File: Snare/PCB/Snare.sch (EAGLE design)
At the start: 97 parts, among them IC1 LM741P, IC2 LM741P, IC3 LM741P, IC4 LM741P, IC5 LM741P, IC6 LM741P, Q1 2N3904, Q2 2N3904, Q3 2N2222A, Q4 2N2222A, Q6 2N3904

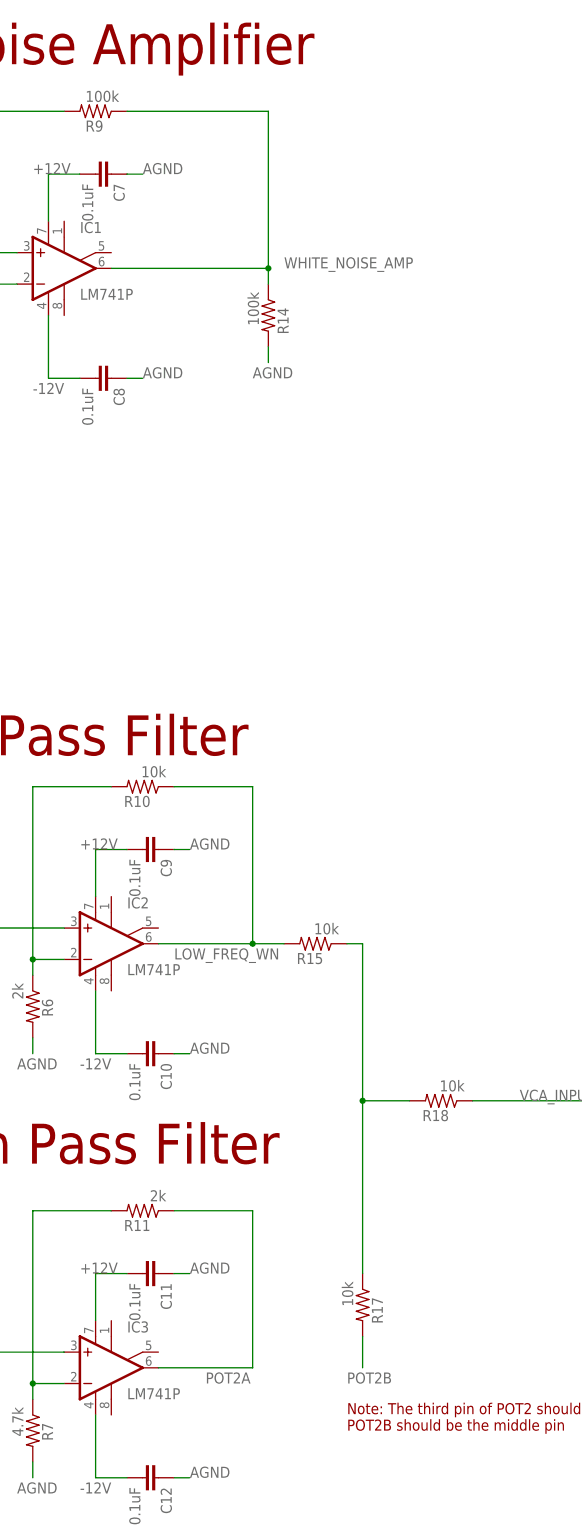
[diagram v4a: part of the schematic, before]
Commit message: Added a few missing components
Added a few missing components. 3 coupling capacitors were missing
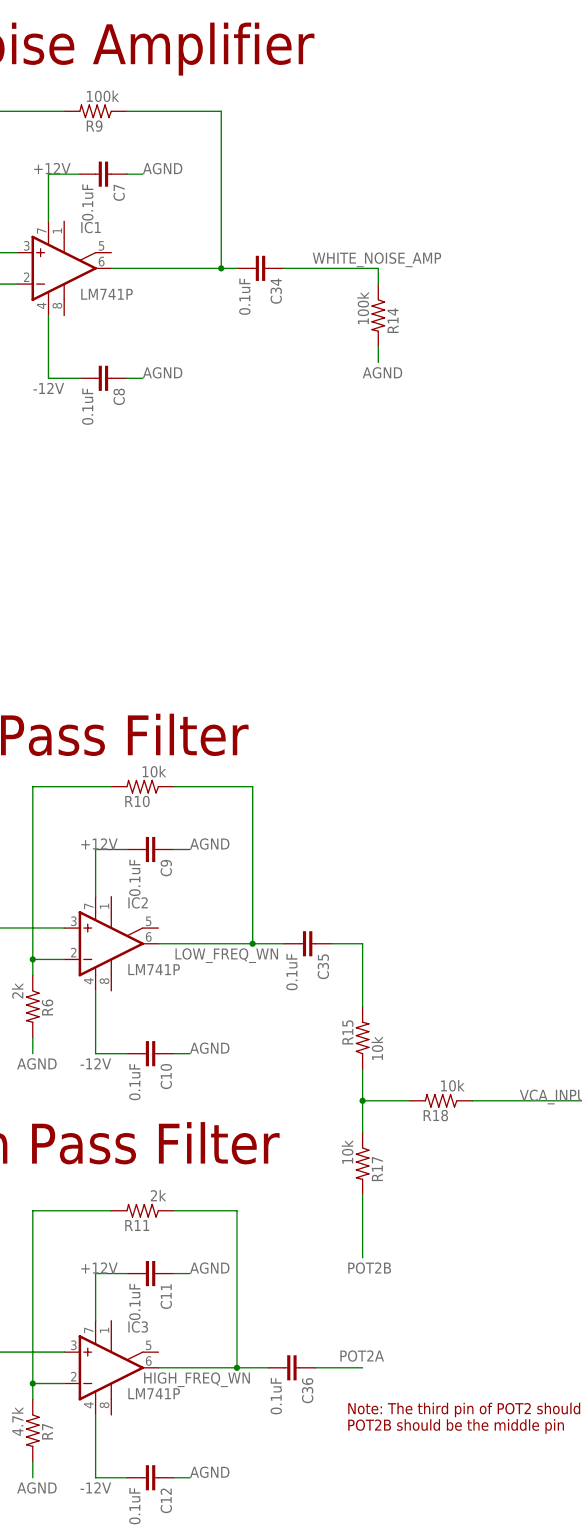
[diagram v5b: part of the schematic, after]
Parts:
- added C34, C35, C36: 0.1uF, resistor:C-EU050-024X044
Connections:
- new net HIGH_FREQ_WN: C36.2, IC3.OUT, R11.1
- new net N$10: C35.1, R15.2
- new net N$9: C34.2, IC1.OUT, R9.1
- net LOW_FREQ_WN: now also C35.2; no longer R15.2
- net POT2A: now also C36.1; no longer IC3.OUT, R11.1
- net WHITE_NOISE_AMP: now also C34.1; no longer IC1.OUT, R9.1
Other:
- moved on the sheet: R14, R15, R17
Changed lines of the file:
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@@
 <part name="J3" library="SparkFun-Connectors" deviceset="CONN_02" device="1X02_NO_SILK"/>
 <part name="J4" library="SparkFun-Connectors" deviceset="CONN_02" device="1X02_NO_SILK"/>
+<part name="C34" library="resistor" library_urn="urn:adsk.eagle:library:348" deviceset="C-EU" device="050-024X044" package3d_urn="urn:adsk.eagle:package:26162/1" value="0.1uF"/>
+<part name="C35" library="resistor" library_urn="urn:adsk.eagle:library:348" deviceset="C-EU" device="050-024X044" package3d_urn="urn:adsk.eagle:package:26162/1" value="0.1uF"/>
+<part name="C36" library="resistor" library_urn="urn:adsk.eagle:library:348" deviceset="C-EU" device="050-024X044" package3d_urn="urn:adsk.eagle:package:26162/1" value="0.1uF"/>
 </parts>
 <sheets>
@@
 <attribute name="VALUE" x="75.438" y="146.05" size="1.778" layer="96" rot="R270"/>
 </instance>
-<instance part="R14" gate="G$1" x="116.84" y="254" smashed="yes" rot="R270">
-<attribute name="NAME" x="118.3386" y="255.27" size="1.778" layer="95" rot="R270"/>
-<attribute name="VALUE" x="113.538" y="257.81" size="1.778" layer="96" rot="R270"/>
-</instance>
-<instance part="R15" gate="G$1" x="124.46" y="152.4" smashed="yes" rot="R180">
-<attribute name="NAME" x="125.73" y="150.9014" size="1.778" layer="95" rot="R180"/>
-<attribute name="VALUE" x="128.27" y="155.702" size="1.778" layer="96" rot="R180"/>
+<instance part="R14" gate="G$1" x="134.62" y="254" smashed="yes" rot="R270">
+<attribute name="NAME" x="136.1186" y="255.27" size="1.778" layer="95" rot="R270"/>
+<attribute name="VALUE" x="131.318" y="257.81" size="1.778" layer="96" rot="R270"/>
+</instance>
+<instance part="R15" gate="G$1" x="132.08" y="137.16" smashed="yes" rot="R90">
+<attribute name="NAME" x="130.5814" y="135.89" size="1.778" layer="95" rot="R90"/>
+<attribute name="VALUE" x="135.382" y="133.35" size="1.778" layer="96" rot="R90"/>
 </instance>
 <instance part="R18" gate="G$1" x="144.78" y="127" smashed="yes" rot="R180">
@@
 <attribute name="VALUE" x="148.59" y="130.302" size="1.778" layer="96" rot="R180"/>
 </instance>
-<instance part="R17" gate="G$1" x="132.08" y="93.98" smashed="yes" rot="R270">
-<attribute name="NAME" x="133.5786" y="95.25" size="1.778" layer="95" rot="R270"/>
-<attribute name="VALUE" x="128.778" y="97.79" size="1.778" layer="96" rot="R270"/>
+<instance part="R17" gate="G$1" x="132.08" y="116.84" smashed="yes" rot="R270">
+<attribute name="NAME" x="133.5786" y="118.11" size="1.778" layer="95" rot="R270"/>
+<attribute name="VALUE" x="128.778" y="120.65" size="1.778" layer="96" rot="R270"/>
 </instance>
 <instance part="IC6" gate="A" x="406.4" y="149.86" smashed="yes">
@@
 <attribute name="VALUE" x="370.84" y="58.674" size="1.778" layer="96" font="vector"/>
 <attribute name="NAME" x="370.84" y="69.088" size="1.778" layer="95" font="vector"/>
+</instance>
+<instance part="C34" gate="G$1" x="116.84" y="261.62" smashed="yes" rot="R270">
+<attribute name="NAME" x="117.221" y="260.096" size="1.778" layer="95" rot="R270"/>
+<attribute name="VALUE" x="112.141" y="260.096" size="1.778" layer="96" rot="R270"/>
+</instance>
+<instance part="C35" gate="G$1" x="124.46" y="152.4" smashed="yes" rot="R270">
+<attribute name="NAME" x="124.841" y="150.876" size="1.778" layer="95" rot="R270"/>
+<attribute name="VALUE" x="119.761" y="150.876" size="1.778" layer="96" rot="R270"/>
+</instance>
+<instance part="C36" gate="G$1" x="121.92" y="83.82" smashed="yes" rot="R270">
+<attribute name="NAME" x="122.301" y="82.296" size="1.778" layer="95" rot="R270"/>
+<attribute name="VALUE" x="117.221" y="82.296" size="1.778" layer="96" rot="R270"/>
 </instance>
 </instances>
@@
 </segment>
 <segment>
-<pinref part="R11" gate="G$1" pin="1"/>
-<wire x1="101.6" y1="109.22" x2="114.3" y2="109.22" width="0.1524" layer="91"/>
-<wire x1="114.3" y1="109.22" x2="114.3" y2="83.82" width="0.1524" layer="91"/>
-<pinref part="IC3" gate="A" pin="OUT"/>
-<wire x1="114.3" y1="83.82" x2="99.06" y2="83.82" width="0.1524" layer="91"/>
-<label x="106.68" y="81.28" size="1.778" layer="95"/>
+<pinref part="C36" gate="G$1" pin="1"/>
+<wire x1="124.46" y1="83.82" x2="132.08" y2="83.82" width="0.1524" layer="91"/>
+<label x="128.27" y="84.836" size="1.778" layer="95"/>
 </segment>
 </net>
@@
 <segment>
 <pinref part="R17" gate="G$1" pin="2"/>
-<wire x1="132.08" y1="88.9" x2="132.08" y2="83.82" width="0.1524" layer="91"/>
-<label x="129.54" y="81.28" size="1.778" layer="95"/>
+<wire x1="132.08" y1="111.76" x2="132.08" y2="101.6" width="0.1524" layer="91"/>
+<label x="129.54" y="99.06" size="1.778" layer="95"/>
 </segment>
 </net>
@@
 <segment>
 <pinref part="R14" gate="G$1" pin="2"/>
-<wire x1="116.84" y1="248.92" x2="116.84" y2="246.38" width="0.1524" layer="91"/>
-<label x="114.3" y="243.84" size="1.778" layer="95"/>
+<wire x1="134.62" y1="248.92" x2="134.62" y2="246.38" width="0.1524" layer="91"/>
+<label x="132.08" y="243.84" size="1.778" layer="95"/>
 </segment>
 <segment>
@@
 <net name="WHITE_NOISE_AMP" class="0">
 <segment>
-<pinref part="R9" gate="G$1" pin="1"/>
-<wire x1="93.98" y1="287.02" x2="116.84" y2="287.02" width="0.1524" layer="91"/>
-<wire x1="116.84" y1="287.02" x2="116.84" y2="261.62" width="0.1524" layer="91"/>
-<pinref part="IC1" gate="A" pin="OUT"/>
-<wire x1="116.84" y1="261.62" x2="91.44" y2="261.62" width="0.1524" layer="91"/>
-<label x="119.38" y="261.62" size="1.778" layer="95"/>
-<pinref part="R14" gate="G$1" pin="1"/>
-<wire x1="116.84" y1="261.62" x2="116.84" y2="259.08" width="0.1524" layer="91"/>
-<junction x="116.84" y="261.62"/>
-</segment>
-<segment>
 <pinref part="C2" gate="G$1" pin="2"/>
 <wire x1="50.8" y1="86.36" x2="48.26" y2="86.36" width="0.1524" layer="91"/>
@@
 <wire x1="48.26" y1="154.94" x2="45.72" y2="154.94" width="0.1524" layer="91"/>
 <label x="20.32" y="154.94" size="1.778" layer="95"/>
+</segment>
+<segment>
+<pinref part="C34" gate="G$1" pin="1"/>
+<wire x1="119.38" y1="261.62" x2="134.62" y2="261.62" width="0.1524" layer="91"/>
+<pinref part="R14" gate="G$1" pin="1"/>
+<wire x1="134.62" y1="261.62" x2="134.62" y2="259.08" width="0.1524" layer="91"/>
+<label x="123.952" y="262.382" size="1.778" layer="95"/>
 </segment>
 </net>
@@
 <wire x1="114.3" y1="152.4" x2="99.06" y2="152.4" width="0.1524" layer="91"/>
 <label x="101.6" y="149.86" size="1.778" layer="95"/>
-<pinref part="R15" gate="G$1" pin="2"/>
-<wire x1="114.3" y1="152.4" x2="119.38" y2="152.4" width="0.1524" layer="91"/>
+<pinref part="C35" gate="G$1" pin="2"/>
+<wire x1="119.38" y1="152.4" x2="114.3" y2="152.4" width="0.1524" layer="91"/>
 <junction x="114.3" y="152.4"/>
 </segment>
@@
 <net name="N$1" class="0">
 <segment>
-<pinref part="R15" gate="G$1" pin="1"/>
-<wire x1="129.54" y1="152.4" x2="132.08" y2="152.4" width="0.1524" layer="91"/>
-<wire x1="132.08" y1="152.4" x2="132.08" y2="127" width="0.1524" layer="91"/>
 <pinref part="R18" gate="G$1" pin="2"/>
 <wire x1="132.08" y1="127" x2="139.7" y2="127" width="0.1524" layer="91"/>
-<wire x1="132.08" y1="127" x2="132.08" y2="99.06" width="0.1524" layer="91"/>
+<wire x1="132.08" y1="127" x2="132.08" y2="121.92" width="0.1524" layer="91"/>
+<pinref part="R17" gate="G$1" pin="1"/>
+<pinref part="R15" gate="G$1" pin="1"/>
+<wire x1="132.08" y1="132.08" x2="132.08" y2="127" width="0.1524" layer="91"/>
 <junction x="132.08" y="127"/>
-<pinref part="R17" gate="G$1" pin="1"/>
 </segment>
 </net>
@@
 </segment>
 </net>
+<net name="N$9" class="0">
+<segment>
+<pinref part="R9" gate="G$1" pin="1"/>
+<wire x1="93.98" y1="287.02" x2="109.22" y2="287.02" width="0.1524" layer="91"/>
+<wire x1="109.22" y1="287.02" x2="109.22" y2="261.62" width="0.1524" layer="91"/>
+<pinref part="IC1" gate="A" pin="OUT"/>
+<wire x1="109.22" y1="261.62" x2="91.44" y2="261.62" width="0.1524" layer="91"/>
+<pinref part="C34" gate="G$1" pin="2"/>
+<wire x1="109.22" y1="261.62" x2="111.76" y2="261.62" width="0.1524" layer="91"/>
+<junction x="109.22" y="261.62"/>
+</segment>
+</net>
+<net name="N$10" class="0">
+<segment>
+<pinref part="C35" gate="G$1" pin="1"/>
+<wire x1="127" y1="152.4" x2="132.08" y2="152.4" width="0.1524" layer="91"/>
+<pinref part="R15" gate="G$1" pin="2"/>
+<wire x1="132.08" y1="152.4" x2="132.08" y2="142.24" width="0.1524" layer="91"/>
+</segment>
+</net>
+<net name="HIGH_FREQ_WN" class="0">
+<segment>
+<pinref part="R11" gate="G$1" pin="1"/>
+<wire x1="101.6" y1="109.22" x2="111.76" y2="109.22" width="0.1524" layer="91"/>
+<wire x1="111.76" y1="109.22" x2="111.76" y2="83.82" width="0.1524" layer="91"/>
+<pinref part="C36" gate="G$1" pin="2"/>
+<wire x1="111.76" y1="83.82" x2="116.84" y2="83.82" width="0.1524" layer="91"/>
+<pinref part="IC3" gate="A" pin="OUT"/>
+<wire x1="111.76" y1="83.82" x2="99.06" y2="83.82" width="0.1524" layer="91"/>
+<junction x="111.76" y="83.82"/>
+<label x="96.52" y="81.28" size="1.778" layer="95"/>
+</segment>
+</net>

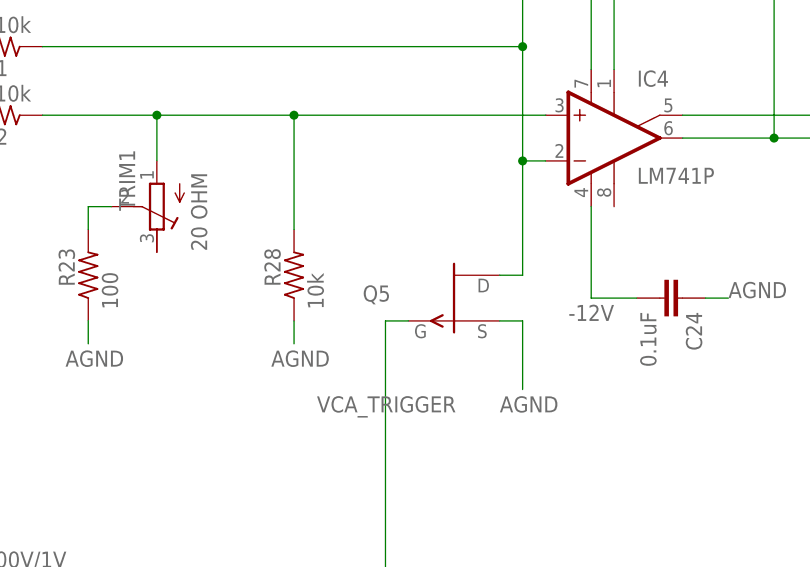
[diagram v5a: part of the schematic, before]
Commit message: Made a change to the schematic
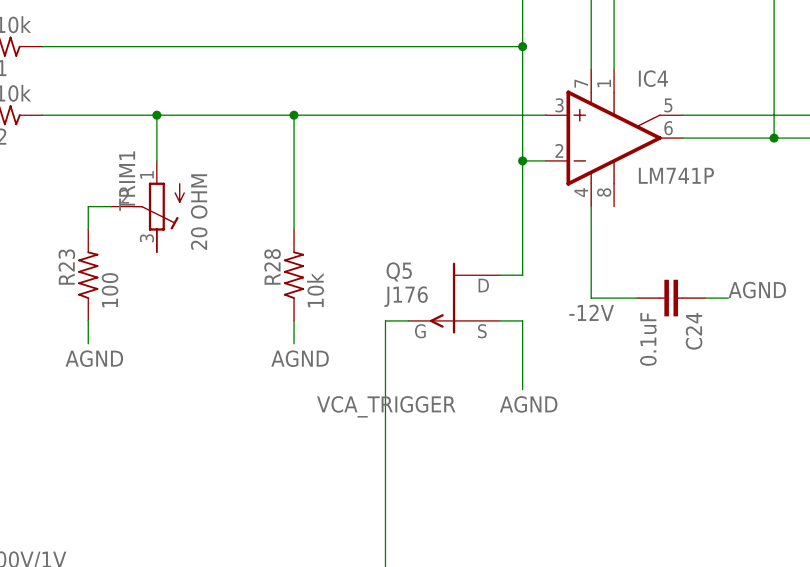
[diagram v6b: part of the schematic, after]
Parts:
- Q5: value (none) -> J176
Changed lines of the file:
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@@
 <part name="C21" library="resistor" library_urn="urn:adsk.eagle:library:348" deviceset="C-EU" device="050-024X044" package3d_urn="urn:adsk.eagle:package:26162/1" value="0.1uF"/>
 <part name="TRIM2" library="rcl" library_urn="urn:adsk.eagle:library:334" deviceset="R-TRIMM" device="64W" package3d_urn="urn:adsk.eagle:package:23748/1" value="10k"/>
-<part name="Q5" library="Capstone" deviceset="J176" device=""/>
+<part name="Q5" library="Capstone" deviceset="J176" device="" value="J176"/>
 <part name="R21" library="resistor" library_urn="urn:adsk.eagle:library:348" deviceset="R-US_" device="0207/10" package3d_urn="urn:adsk.eagle:package:25939/1" value="10k"/>
 <part name="R22" library="resistor" library_urn="urn:adsk.eagle:library:348" deviceset="R-US_" device="0207/10" package3d_urn="urn:adsk.eagle:package:25939/1" value="10k"/>
@@
 </instance>
 <instance part="Q5" gate="G$1" x="269.24" y="121.92" smashed="yes" rot="MR180">
-<attribute name="NAME" x="259.08" y="123.317" size="1.778" layer="95" rot="MR180"/>
-<attribute name="VALUE" x="259.08" y="125.73" size="1.778" layer="96" rot="MR180"/>
+<attribute name="NAME" x="261.62" y="125.857" size="1.778" layer="95" rot="MR180"/>
+<attribute name="VALUE" x="261.62" y="123.19" size="1.778" layer="96" rot="MR180"/>
 </instance>
 <instance part="R21" gate="G$1" x="218.44" y="149.86" smashed="yes" rot="R180">
